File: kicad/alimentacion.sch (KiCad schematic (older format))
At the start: 19 parts, among them P3 aliment., P4 sw_aliment, P5 sw_pic, P6 CONN_01X03, P7 CONN_01X03, U1 LM78L05ACZ, U2 LM7805CT

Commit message: cambios menores
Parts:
- D2, D4: symbol LED -> LED-RESCUE-np08
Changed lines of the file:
@@
 EESchema Schematic File Version 2
+LIBS:np08-rescue
 LIBS:power
 LIBS:device
@@
 $EndComp
 $Comp
-L LED D2
+L LED-RESCUE-np08 D2
 U 1 1 579A692B
 P 6700 4000
@@
 $EndComp
 $Comp
-L LED D4
+L LED-RESCUE-np08 D4
 U 1 1 579B97B7
 P 6900 2650

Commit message: cambios en la placa np08
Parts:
- removed D2, D4: LED, LEDs:LED-5MM, symbol LED-RESCUE-np08
- removed D5: D, Diodes_ThroughHole:Diode_DO-35_SOD27_Horizontal_RM10, symbol D
- removed P5: sw_pic, Pin_Headers:Pin_Header_Straight_1x03, symbol CONN_01X03
- removed P6, P7: CONN_01X03, Pin_Headers:Pin_Header_Straight_1x03, symbol CONN_01X03
- removed R3, R4: 470, Resistors_ThroughHole:Resistor_Horizontal_RM15mm, symbol R
- C10: renamed from C8; footprint Capacitors_ThroughHole:C_Disc_D3_P2.5 -> Capacitors_THT:C_Disc_D3.4mm_W2.1mm_P2.50mm
- C11: footprint Capacitors_ThroughHole:C_Disc_D3_P2.5 -> Capacitors_THT:C_Disc_D3.4mm_W2.1mm_P2.50mm
- C6: renamed from C9; footprint Capacitors_ThroughHole:C_Radial_D5_L6_P2.5 -> Capacitors_THT:CP_Radial_D6.3mm_P2.50mm
- C7: renamed from C6; footprint Capacitors_ThroughHole:C_Radial_D5_L6_P2.5 -> Capacitors_THT:CP_Radial_D6.3mm_P2.50mm
- C8: renamed from C10; footprint Capacitors_ThroughHole:C_Radial_D5_L6_P2.5 -> Capacitors_THT:CP_Radial_D6.3mm_P2.50mm
- C9: renamed from C7; footprint Capacitors_ThroughHole:C_Radial_D5_L6_P2.5 -> Capacitors_THT:CP_Radial_D6.3mm_P2.50mm
- D2: renamed from D3; footprint Diodes_ThroughHole:Diode_DO-35_SOD27_Horizontal_RM10 -> Diodes_THT:D_5W_P12.70mm_Horizontal
- P6: renamed from P4; footprint Pin_Headers:Pin_Header_Straight_1x03 -> Pin_Headers:Pin_Header_Straight_1x03_Pitch2.54mm
- P7: renamed from P3; footprint Connect:bornier2 -> Connectors:bornier2
- U1: renamed from U2; footprint TO_SOT_Packages_THT:TO-220_Neutral123_Horizontal -> TO_SOT_Packages_THT:TO-220_Horizontal
- renumbered U1 to U2

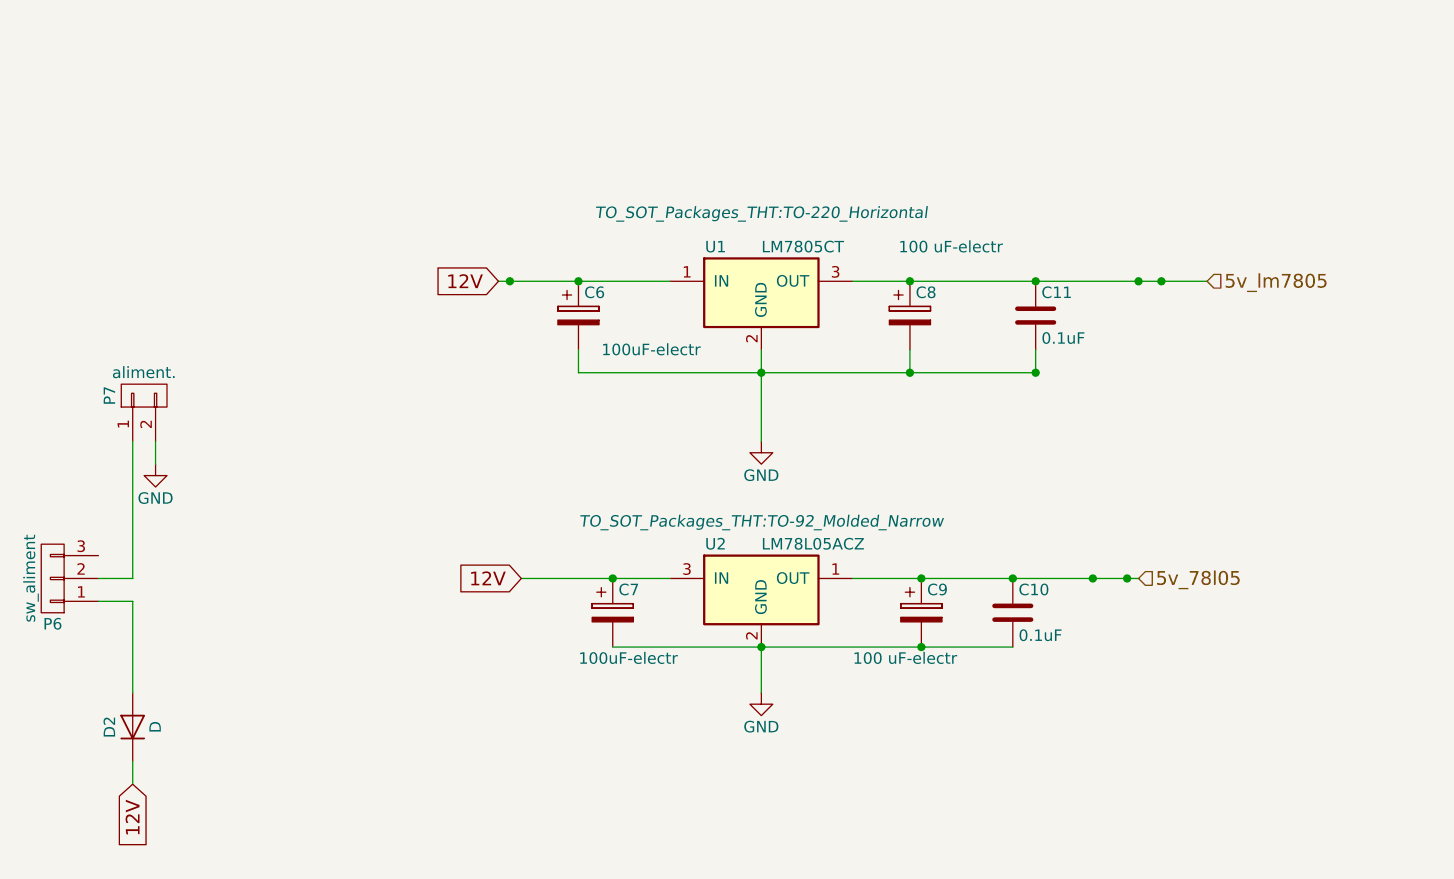
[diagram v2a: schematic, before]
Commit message: arreglando la fuente de alimentación, los servos estaban conectados al 78l05
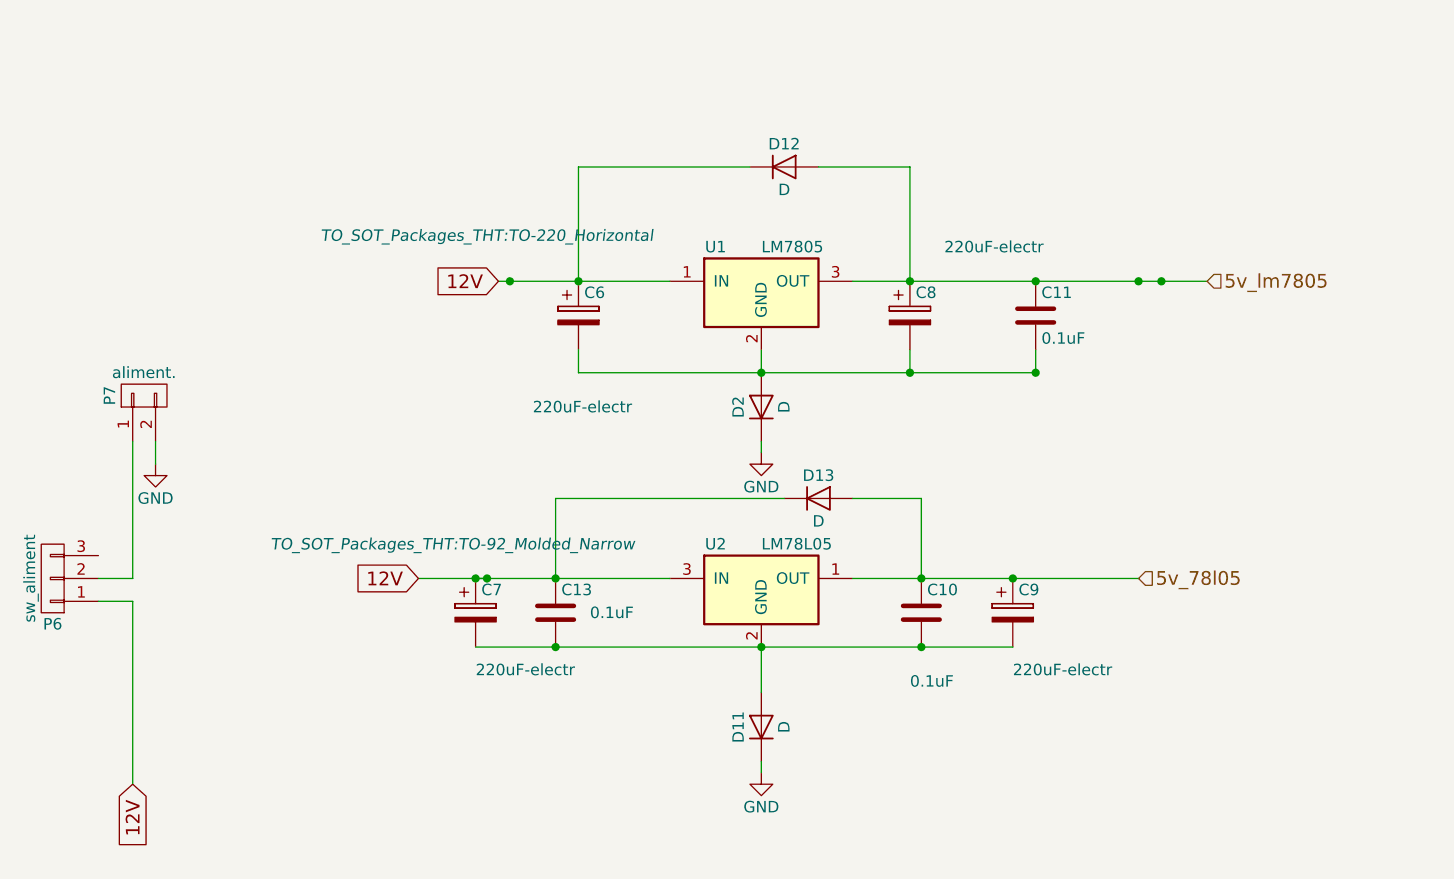
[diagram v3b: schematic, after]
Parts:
- added C13: 0.1uF, Capacitors_THT:C_Disc_D3.4mm_W2.1mm_P2.50mm, symbol C
- added D11, D12, D13: D, Diodes_THT:D_T-1_P5.08mm_Horizontal, symbol D
- C6, C7: value 100uF-electr -> 220uF-electr
- C8, C9: value 100 uF-electr -> 220uF-electr
- D2: footprint Diodes_THT:D_5W_P12.70mm_Horizontal -> Diodes_THT:D_T-1_P5.08mm_Horizontal
- U1: value LM7805CT -> LM7805
- U2: value LM78L05ACZ -> LM78L05
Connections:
- net 12V: now also P6.1 (P1), C13.1, D12.1 (K), D13.1 (K); no longer D2.1 (K)
- net 5v_78l05: now also D13.2 (A)
- net 5v_lm7805: now also D12.2 (A)
- net GND: now also D2.1 (K), D11.1 (K); no longer C10.2, C11.2, C6.2, C7.2, C8.2, C9.2, U1.2 (GND), U2.2 (GND)
- net at D2.2 (A): now also C11.2, C6.2, C8.2, U1.2 (GND); no longer P6.1 (P1)
- new net: C10.2, C13.2, C7.2, C9.2, D11.2 (A), U2.2 (GND)
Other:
- moved on the sheet: C10, C7, C9
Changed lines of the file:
@@
 L C C10
 U 1 1 579A683E
+P 5950 3450
+F 0 "C10" H 5975 3550 50  0000 L CNN
+F 1 "0.1uF" H 5900 3150 50  0000 L CNN
+F 2 "Capacitors_THT:C_Disc_D3.4mm_W2.1mm_P2.50mm" H 5988 3300 50  0001 C CNN
+F 3 "" H 5950 3450 50  0000 C CNN
+	1    5950 3450
+	1    0    0    -1
+$EndComp
+$Comp
+L CP C9
+U 1 1 579A68A5
 P 6350 3450
-F 0 "C10" H 6375 3550 50  0000 L CNN
-F 1 "0.1uF" H 6375 3350 50  0000 L CNN
-F 2 "Capacitors_THT:C_Disc_D3.4mm_W2.1mm_P2.50mm" H 6388 3300 50  0001 C CNN
+F 0 "C9" H 6375 3550 50  0000 L CNN
+F 1 "220uF-electr" H 6350 3200 50  0000 L CNN
+F 2 "Capacitors_THT:CP_Radial_D6.3mm_P2.50mm" H 6388 3300 50  0001 C CNN
 F 3 "" H 6350 3450 50  0000 C CNN
 	1    6350 3450
@@
 $EndComp
 $Comp
-L CP C9
-U 1 1 579A68A5
-P 5950 3450
-F 0 "C9" H 5975 3550 50  0000 L CNN
-F 1 "100 uF-electr" H 5650 3250 50  0000 L CNN
-F 2 "Capacitors_THT:CP_Radial_D6.3mm_P2.50mm" H 5988 3300 50  0001 C CNN
-F 3 "" H 5950 3450 50  0000 C CNN
-	1    5950 3450
-	1    0    0    -1
-$EndComp
-$Comp
 L CP C7
 U 1 1 579A68DB
-P 4600 3450
-F 0 "C7" H 4625 3550 50  0000 L CNN
-F 1 "100uF-electr" H 4450 3250 50  0000 L CNN
-F 2 "Capacitors_THT:CP_Radial_D6.3mm_P2.50mm" H 4638 3300 50  0001 C CNN
-F 3 "" H 4600 3450 50  0000 C CNN
-	1    4600 3450
-	1    0    0    -1
-$EndComp
-$Comp
-L GND #PWR027
+P 4000 3450
+F 0 "C7" H 4025 3550 50  0000 L CNN
+F 1 "220uF-electr" H 4000 3200 50  0000 L CNN
+F 2 "Capacitors_THT:CP_Radial_D6.3mm_P2.50mm" H 4038 3300 50  0001 C CNN
+F 3 "" H 4000 3450 50  0000 C CNN
+	1    4000 3450
+	1    0    0    -1
+$EndComp
+$Comp
+L GND #PWR021
 U 1 1 579A6B49
-P 5250 3800
-F 0 "#PWR027" H 5250 3550 50  0001 C CNN
-F 1 "GND" H 5250 3650 50  0000 C CNN
-F 2 "" H 5250 3800 50  0000 C CNN
-F 3 "" H 5250 3800 50  0000 C CNN
-	1    5250 3800
+P 5250 4150
+F 0 "#PWR021" H 5250 3900 50  0001 C CNN
+F 1 "GND" H 5250 4000 50  0000 C CNN
+F 2 "" H 5250 4150 50  0000 C CNN
+F 3 "" H 5250 4150 50  0000 C CNN
+	1    5250 4150
 	1    0    0    -1
 $EndComp
 Text HLabel 6900 3300 2    60   Input ~ 0
 5v_78l05
-Text GLabel 4200 3300 0    60   Input ~ 0
+Text GLabel 3750 3300 0    60   Input ~ 0
 12V
 $Comp
@@
 12V
 $Comp
-L GND #PWR028
+L GND #PWR022
 U 1 1 579A71F1
 P 2600 2800
-F 0 "#PWR028" H 2600 2550 50  0001 C CNN
+F 0 "#PWR022" H 2600 2550 50  0001 C CNN
 F 1 "GND" H 2600 2650 50  0000 C CNN
 F 2 "" H 2600 2800 50  0000 C CNN
@@
 P 5250 3350
 F 0 "U2" H 5050 3550 50  0000 C CNN
-F 1 "LM78L05ACZ" H 5250 3550 50  0000 L CNN
-F 2 "TO_SOT_Packages_THT:TO-92_Molded_Narrow" H 5250 3650 50  0000 C CIN
+F 1 "LM78L05" H 5250 3550 50  0000 L CNN
+F 2 "TO_SOT_Packages_THT:TO-92_Molded_Narrow" H 3900 3550 50  0000 C CIN
 F 3 "" H 5250 3350 50  0000 C CNN
 	1    5250 3350
@@
 P 5250 2050
 F 0 "U1" H 5050 2250 50  0000 C CNN
-F 1 "LM7805CT" H 5250 2250 50  0000 L CNN
-F 2 "TO_SOT_Packages_THT:TO-220_Horizontal" H 5250 2400 50  0000 C CIN
+F 1 "LM7805" H 5250 2250 50  0000 L CNN
+F 2 "TO_SOT_Packages_THT:TO-220_Horizontal" H 4050 2300 50  0000 C CIN
 F 3 "" H 5250 2050 50  0000 C CNN
 	1    5250 2050
@@
 P 4450 2150
 F 0 "C6" H 4475 2250 50  0000 L CNN
-F 1 "100uF-electr" H 4550 2000 50  0000 L CNN
+F 1 "220uF-electr" H 4250 1750 50  0000 L CNN
 F 2 "Capacitors_THT:CP_Radial_D6.3mm_P2.50mm" H 4488 2000 50  0001 C CNN
 F 3 "" H 4450 2150 50  0000 C CNN
@@
 P 5900 2150
 F 0 "C8" H 5925 2250 50  0000 L CNN
-F 1 "100 uF-electr" H 5850 2450 50  0000 L CNN
+F 1 "220uF-electr" H 6050 2450 50  0000 L CNN
 F 2 "Capacitors_THT:CP_Radial_D6.3mm_P2.50mm" H 5938 2000 50  0001 C CNN
 F 3 "" H 5900 2150 50  0000 C CNN
@@
 $EndComp
 $Comp
-L GND #PWR029
+L GND #PWR023
 U 1 1 579B987F
-P 5250 2700
-F 0 "#PWR029" H 5250 2450 50  0001 C CNN
-F 1 "GND" H 5250 2550 50  0000 C CNN
-F 2 "" H 5250 2700 50  0000 C CNN
-F 3 "" H 5250 2700 50  0000 C CNN
-	1    5250 2700
+P 5250 2750
+F 0 "#PWR023" H 5250 2500 50  0001 C CNN
+F 1 "GND" H 5250 2600 50  0000 C CNN
+F 2 "" H 5250 2750 50  0000 C CNN
+F 3 "" H 5250 2750 50  0000 C CNN
+	1    5250 2750
 	1    0    0    -1
 $EndComp
@@
 $EndComp
 $Comp
+L D D11
+U 1 1 59C18FCD
+P 5250 3950
+F 0 "D11" H 5250 4050 50  0000 C CNN
+F 1 "D" H 5250 3850 50  0000 C CNN
+F 2 "Diodes_THT:D_T-1_P5.08mm_Horizontal" H 5250 3950 50  0001 C CNN
+F 3 "" H 5250 3950 50  0001 C CNN
+	1    5250 3950
+	0    -1   -1   0
+$EndComp
+$Comp
+L D D12
+U 1 1 59C18E9B
+P 5350 1500
+F 0 "D12" H 5350 1600 50  0000 C CNN
+F 1 "D" H 5350 1400 50  0000 C CNN
+F 2 "Diodes_THT:D_T-1_P5.08mm_Horizontal" H 5350 1500 50  0001 C CNN
+F 3 "" H 5350 1500 50  0001 C CNN
+	1    5350 1500
+	1    0    0    -1
+$EndComp
+$Comp
+L D D13
+U 1 1 59C19FEB
+P 5500 2950
+F 0 "D13" H 5500 3050 50  0000 C CNN
+F 1 "D" H 5500 2850 50  0000 C CNN
+F 2 "Diodes_THT:D_T-1_P5.08mm_Horizontal" H 5500 2950 50  0001 C CNN
+F 3 "" H 5500 2950 50  0001 C CNN
+	1    5500 2950
+	1    0    0    -1
+$EndComp
+$Comp
+L C C13
+U 1 1 59C1A116
+P 4350 3450
+F 0 "C13" H 4375 3550 50  0000 L CNN
+F 1 "0.1uF" H 4500 3450 50  0000 L CNN
+F 2 "Capacitors_THT:C_Disc_D3.4mm_W2.1mm_P2.50mm" H 4388 3300 50  0001 C CNN
+F 3 "" H 4350 3450 50  0000 C CNN
+	1    4350 3450
+	1    0    0    -1
+$EndComp
+$Comp
 L D D2
-U 1 1 579B9E2F
-P 2500 3950
-F 0 "D2" H 2500 4050 50  0000 C CNN
-F 1 "D" H 2500 3850 50  0000 C CNN
-F 2 "Diodes_THT:D_5W_P12.70mm_Horizontal" H 2500 3950 50  0001 C CNN
-F 3 "" H 2500 3950 50  0000 C CNN
-	1    2500 3950
+U 1 1 59C1A752
+P 5250 2550
+F 0 "D2" H 5250 2650 50  0000 C CNN
+F 1 "D" H 5250 2450 50  0000 C CNN
+F 2 "Diodes_THT:D_T-1_P5.08mm_Horizontal" H 5250 2550 50  0001 C CNN
+F 3 "" H 5250 2550 50  0001 C CNN
+	1    5250 2550
 	0    -1   -1   0
 $EndComp
@@
 Wire Wire Line
 	5650 3300 6900 3300
-Connection ~ 6700 3300
 Connection ~ 6350 3300
 Connection ~ 5950 3300
-Wire Wire Line
-	4600 3600 6350 3600
 Connection ~ 5950 3600
 Wire Wire Line
@@
 Connection ~ 5250 3600
 Wire Wire Line
-	4200 3300 4850 3300
-Connection ~ 4600 3300
+	3750 3300 4850 3300
 Wire Wire Line
 	6450 2400 6450 2300
@@
 Connection ~ 5900 2000
 Wire Wire Line
-	5250 2700 5250 2300
-Wire Wire Line
 	4100 2000 4850 2000
 Connection ~ 5250 2400
@@
 Connection ~ 6900 2000
 Wire Wire Line
-	2500 4200 2500 4100
-Wire Wire Line
 	2500 3300 2350 3300
 Wire Wire Line
 	2350 3400 2500 3400
 Wire Wire Line
-	2500 3400 2500 3800
-Wire Wire Line
 	4450 2400 6450 2400
-Connection ~ 6850 3300
 Connection ~ 7000 2000
 Connection ~ 4150 2000
+Wire Wire Line
+	2500 3400 2500 4200
+Wire Wire Line
+	5650 2950 5950 2950
+Wire Wire Line
+	5950 2950 5950 3300
+Wire Wire Line
+	4350 2950 5350 2950
+Wire Wire Line
+	4350 2950 4350 3300
+Connection ~ 4350 3300
+Connection ~ 4350 3600
+Wire Wire Line
+	5500 1500 5900 1500
+Wire Wire Line
+	5900 1500 5900 2000
+Wire Wire Line
+	5200 1500 4450 1500
+Wire Wire Line
+	4450 1500 4450 2000
+Wire Wire Line
+	5250 2400 5250 2300
+Wire Wire Line
+	4000 3600 6350 3600
+Wire Wire Line
+	4000 3300 4050 3300
+Connection ~ 4050 3300
+Connection ~ 4000 3300
+Wire Wire Line
+	5250 4150 5250 4100
+Wire Wire Line
+	5250 2750 5250 2700
 $EndSCHEMATC
